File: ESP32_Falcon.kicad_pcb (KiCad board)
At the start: 2 copper layers, 28 parts, among them J1 USB_C_Receptacle_USB2.0_16P, J2 Conn_01x20_Pin, J3 Conn_01x20_Pin, U1 ESP32-S3-WROOM-1, U2 USBLC6-2SC6, U3 AMS1117-3.3, U4 BMI270

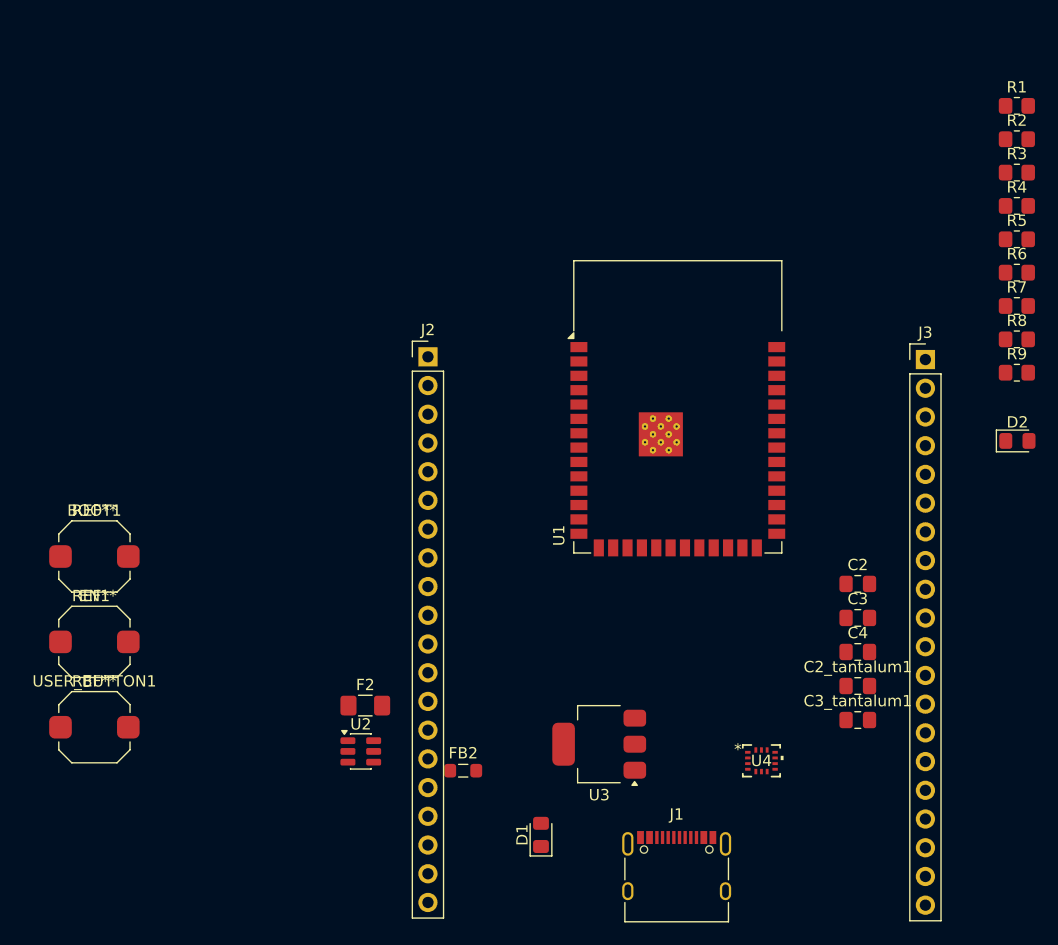
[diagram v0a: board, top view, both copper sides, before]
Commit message: Podlaczone glowne sciezki
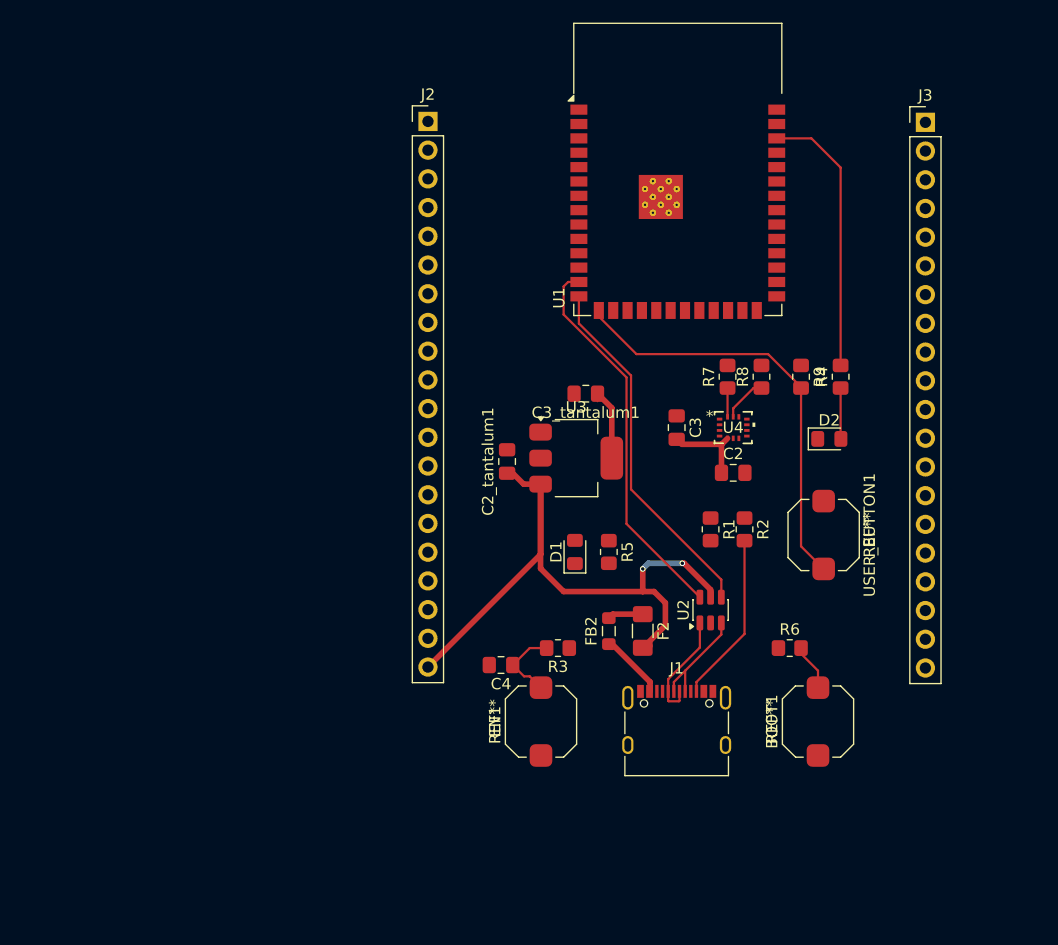
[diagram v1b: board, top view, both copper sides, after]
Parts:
- moved USER_BUTTON1 66.7 mm to (152.0, 80.5), turned to -90 degrees
- moved BOOT1 65.6 mm to (151.5, 97.0), turned to 90 degrees
- moved R3 58.4 mm to (128.5, 90.5), turned to 180 degrees
- moved R1 46.2 mm to (142.0, 80.0), turned to -90 degrees
- moved R5 45.5 mm to (133.0, 82.0), turned to -90 degrees
- moved R2 42.1 mm to (145.0, 80.0), turned to -90 degrees
- moved EN1 40.1 mm to (127.0, 97.0), turned to 90 degrees
- moved R6 38.8 mm to (149.0, 90.5)
- moved C3_tantalum1 37.6 mm to (131.0, 68.0), turned to 180 degrees
- moved C2_tantalum1 36.8 mm to (124.0, 74.0), turned to 90 degrees
- moved U2 33.4 mm to (142.0, 87.1), turned to 90 degrees
- moved C4 31.6 mm to (123.5, 92.0), turned to 180 degrees
- moved U4 29.6 mm to (144.0, 71.0)
- moved R7 26.3 mm to (143.5, 66.5), turned to 90 degrees
- moved F2 25.4 mm to (136.0, 89.0), turned to -90 degrees
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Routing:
- net +5V: track 0.00 -> 58.3 mm, vias 0 -> 2
- net USER_BUTTON: track 0.00 -> 37.9 mm
- net USB_D-: track 0.00 -> 34.0 mm
- net USB_D+: track 0.00 -> 31.8 mm
- net USER_LED: track 0.00 -> 24.2 mm
- net Net-(J1-CC2): track 0.00 -> 15.1 mm
- net +3V3: track 0.00 -> 14.8 mm
- net Net-(J1-D--PadA7): track 0.00 -> 9.91 mm
- net Net-(J1-D+-PadA6): track 0.00 -> 9.62 mm
- net Net-(U1-EN): track 0.00 -> 6.95 mm
- net +5VP: track 0.00 -> 5.86 mm
- net Net-(D2-A): track 0.00 -> 4.51 mm
- net Net-(U1-IO0): track 0.00 -> 4.12 mm
- net Net-(U4-SCX): track 0.00 -> 3.99 mm
- net Net-(F2-Pad1): track 0.00 -> 3.14 mm
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
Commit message: skończony projekt
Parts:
- J2, J3: value Conn_01x20_Pin -> Conn_01x15_Pin; footprint Connector_PinHeader_2.54mm:PinHeader_1x20_P2.54mm_Vertical -> Connector_PinHeader_2.54mm:PinHeader_1x15_P2.54mm_Vertical
- moved C2_tantalum 1.00 mm to (123.0, 74.0)
- moved D1 0.50 mm to (129.5, 82.0)
- moved J3 0.50 mm to (161.0, 43.5)
- moved J2 0.42 mm to (117.0, 43.5)
- turned R9 to 90 degrees
- renumbered C2_tantalum1 to C2_tantalum, C3_tantalum1 to C3_tantalum
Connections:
- J2 pad 1: unconnected-(J2-Pin_1-Pad1) -> +5V
- J2 pad 10: GPIO35 -> GND
- J2 pad 11: GPIO34 -> GPIO18
- J2 pad 12: GPIO11 -> unconnected-(J2-Pin_12-Pad12)
- J2 pad 13: GPIO10 -> GPIO23
- J2 pad 14: RX -> GPIO22
- J2 pad 15: TX -> GPIO21
- J2 pad 2: unconnected-(J2-Pin_2-Pad2) -> +3V3
- J2 pad 3: unconnected-(J2-Pin_3-Pad3) -> GND
- J2 pad 4: unconnected-(J2-Pin_4-Pad4) -> GPIO4
- J2 pad 5: unconnected-(J2-Pin_5-Pad5) -> GPIO5
- J2 pad 6: GPIO25 -> GPIO6
- J2 pad 7: GPIO24 -> GPIO7
- J2 pad 8: GPIO16 -> GPIO12
- J2 pad 9: GPIO26 -> GPIO17
- J3 pad 1: +5V -> GPIO25
- J3 pad 10: GND -> RX
- J3 pad 11: GPIO18 -> SCL
- J3 pad 12: GPIO19 -> SDA
- J3 pad 13: GPIO20 -> GND
- J3 pad 14: GPIO21 -> +3V3
- J3 pad 15: GPIO22 -> +5V
- J3 pad 2: +3V3 -> GPIO24
- J3 pad 3: GND -> GPIO16
- J3 pad 4: GPIO4 -> GPIO26
- J3 pad 5: GPIO5 -> GPIO35
- J3 pad 6: GPIO6 -> GPIO34
- J3 pad 7: GPIO7 -> GPIO11
- J3 pad 8: GPIO12 -> GPIO10
- J3 pad 9: GPIO17 -> TX
- R8 pad 2: +3V3 -> SCL
- U1 pad 8: GPIO8 -> SDA
- U1 pad 9: GPIO9 -> SCL
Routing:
- net +3V3: track 14.8 -> 158.7 mm, vias 0 -> 4
- net GPIO23: track 0.00 -> 75.9 mm
- net GPIO22: track 0.00 -> 55.0 mm, vias 0 -> 3
- net GPIO10: track 0.00 -> 52.1 mm, vias 0 -> 1
- net +5V: track 58.3 -> 110.2 mm, vias 2 -> 4
- net SDA: track 0.00 -> 51.9 mm, vias 0 -> 4
- net GPIO4: track 0.00 -> 51.9 mm, vias 0 -> 2
- net GPIO11: track 0.00 -> 50.9 mm, vias 0 -> 1
- net Net-(U1-EN): track 6.95 -> 57.3 mm, vias 0 -> 2
- net SCL: track 0.00 -> 48.2 mm, vias 0 -> 2
- net Net-(U1-IO0): track 4.12 -> 51.0 mm, vias 0 -> 4
- net GPIO21: track 0.00 -> 45.9 mm, vias 0 -> 4
- net TX: track 0.00 -> 41.0 mm
- net GPIO16: track 0.00 -> 40.7 mm, vias 0 -> 1
- net GPIO25: track 0.00 -> 34.1 mm
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- added copper zone on B.Cu, net GND
- added copper zone on F.Cu, net GND
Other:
- board outline added: 50 x 61 mm
- board text added: "10"
- board text added: "11"
- board text added: "12"
- board text added: "16"
- board text added: "17"
- board text added: "18"
- board text added: "21"
- board text added: "22"
- board text added: "23"
- board text added: "24"
- board text added: "25"
- board text added: "26"
- board text added: "3.3V"
- board text added: "34"
- board text added: "35"
- board text added: "4"
- board text added: "5"
- board text added: "5V"
- board text added: "6"
- board text added: "7"
- board text added: "ESP32_FALCON P.K 275515 v1.0"
- board text added: "GND"
- board text added: "RX"
- board text added: "SCL"
- board text added: "SDA"
- board text added: "TX"
- board text added: "X"
